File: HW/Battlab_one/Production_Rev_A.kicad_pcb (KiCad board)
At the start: 2 copper layers, 68.1 x 50.5 mm, 51 parts, among them IC2 MIC5225-5.0YM5-TR, J1 BANANA_CONN, J3 BANANA_CONN, P1 USB_C_Plug, T1 750315371

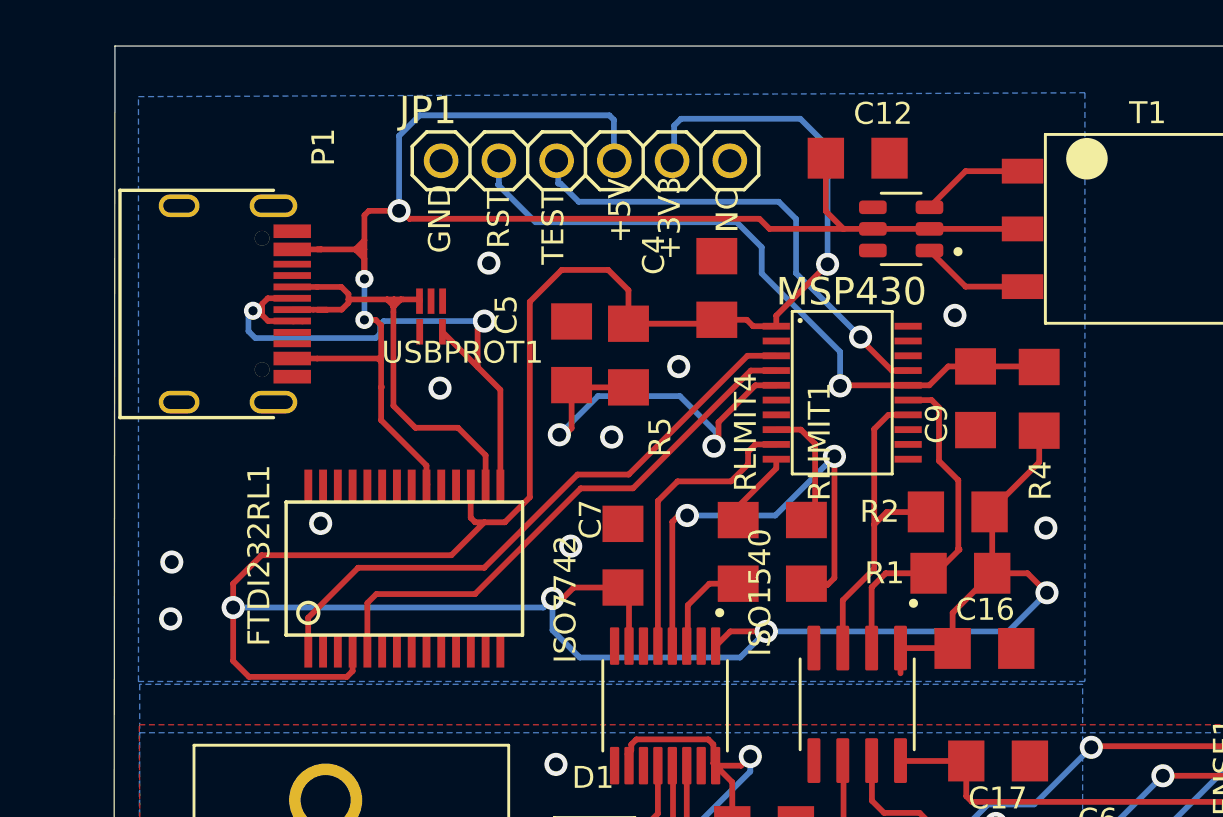
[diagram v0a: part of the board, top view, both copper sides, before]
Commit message: USB-C resistor
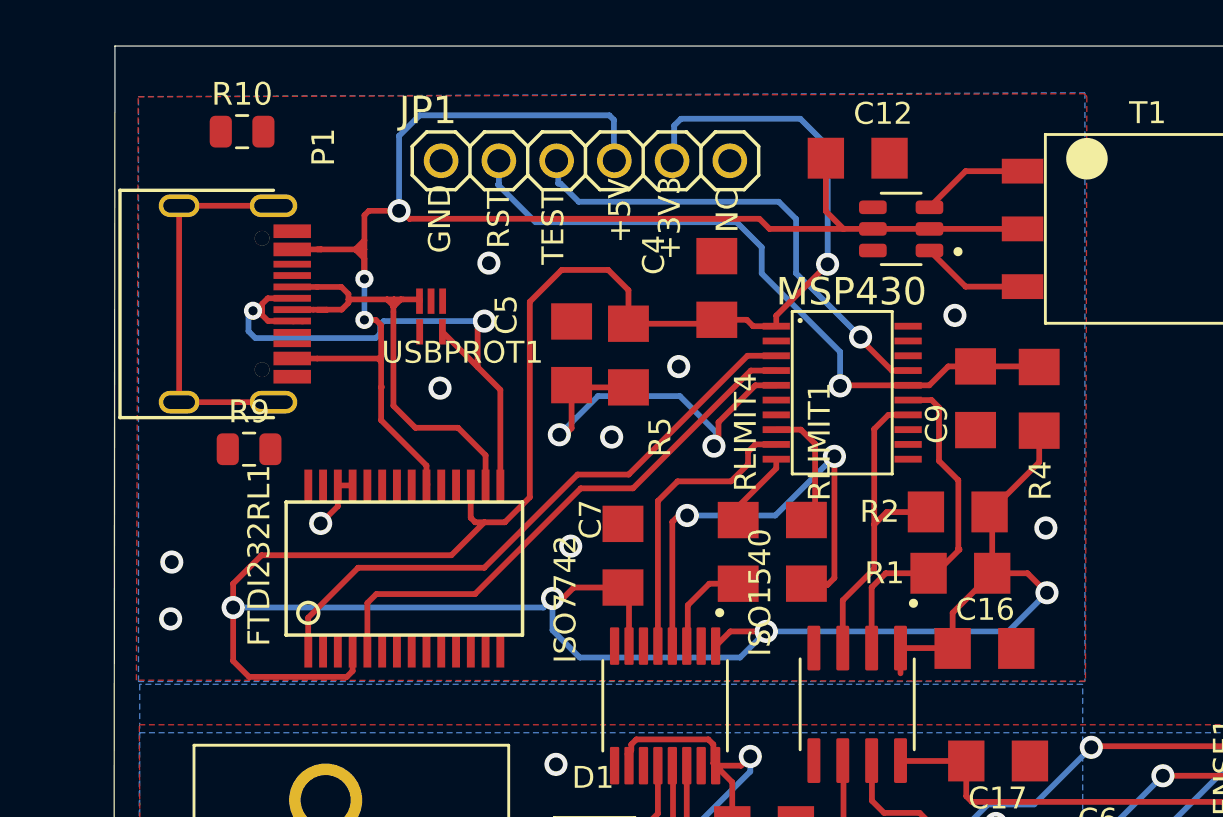
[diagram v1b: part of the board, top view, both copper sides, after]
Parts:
- added R10: 5.1K, Resistor_SMD:R_0805_2012Metric, F.Cu at (120.1, 83.5)
- added R9: 5.1K, Resistor_SMD:R_0805_2012Metric, F.Cu at (120.4, 97.5)
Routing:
- net Net-(P1-PadS1): track 0.00 -> 16.9 mm
- net GND: track 0.00 -> 2.67 mm
- added copper zone on F.Cu, net GND

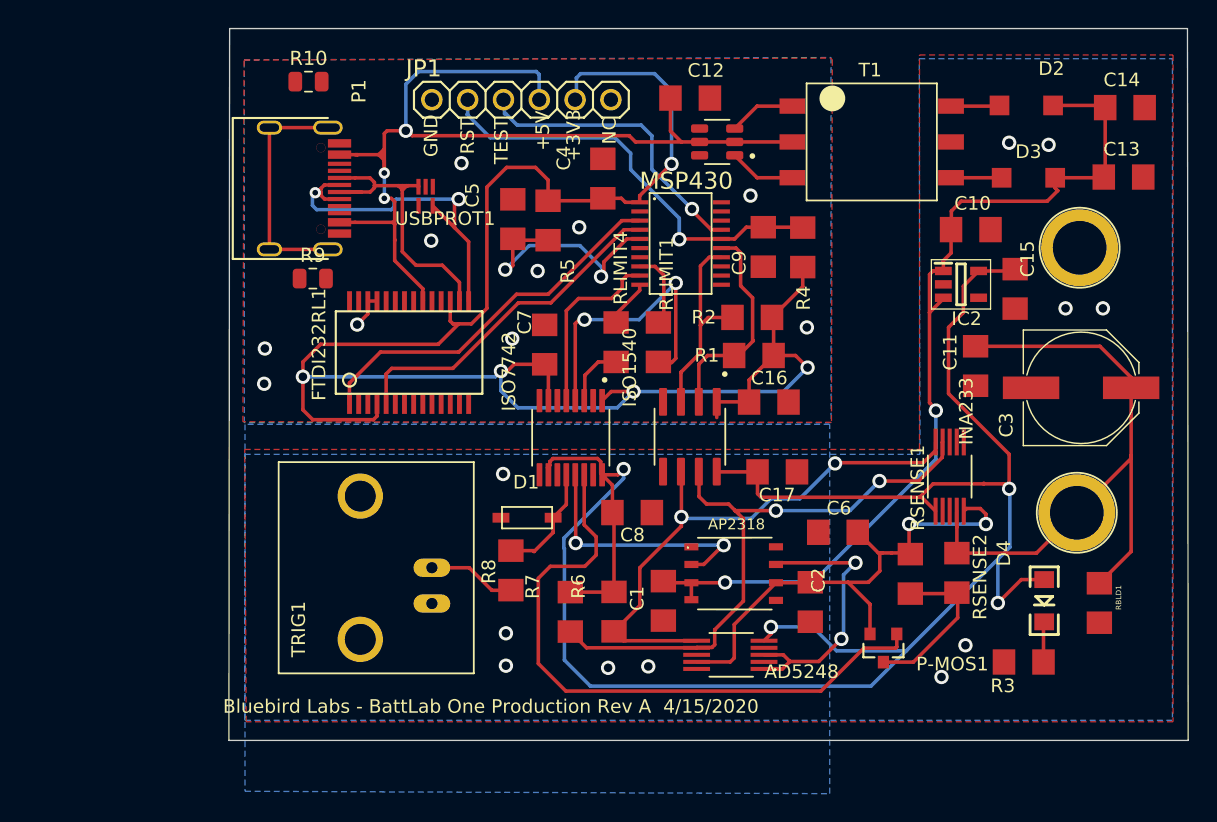
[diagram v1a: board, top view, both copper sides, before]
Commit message: Usb c fixed RTC 0 unconnect
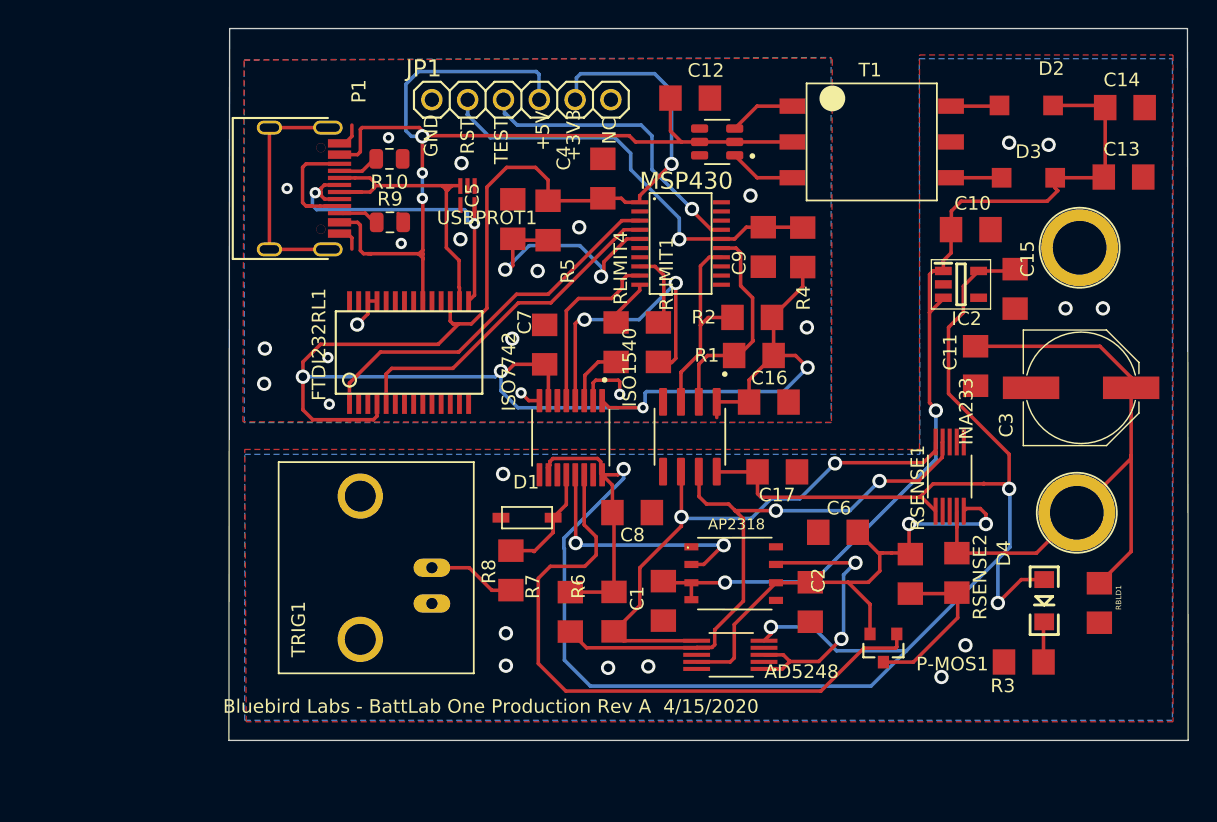
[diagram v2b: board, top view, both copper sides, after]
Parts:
- moved R10 7.94 mm to (125.9, 89.0), turned to 180 degrees
- moved R9 6.77 mm to (125.9, 93.5)
- moved USBPROT1 2.97 mm to (131.4, 91.6)
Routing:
- net GND: track 2.67 -> 12.2 mm, vias 10 -> 17
- net (no net): track 0.00 -> 9.32 mm
- net /VBUS: track 70.8 -> 75.1 mm
- net Net-(P1-PadB5): track 0.00 -> 3.00 mm
- net Net-(P1-PadA5): track 0.00 -> 2.85 mm
- net /D+: track 26.3 -> 24.7 mm
- net Net-(C16-Pad1): track 132.1 -> 133.2 mm
- net /D-: track 21.2 -> 21.9 mm

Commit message: Silkscreen moved
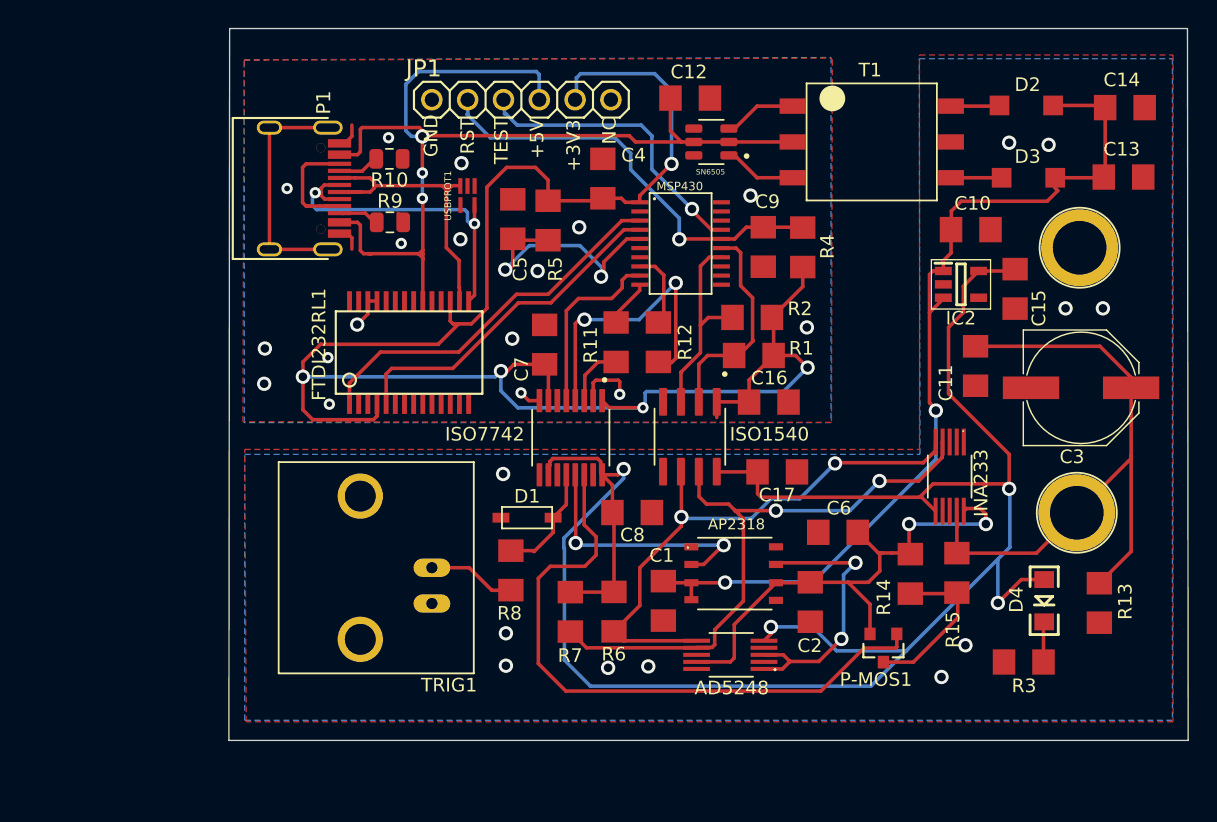
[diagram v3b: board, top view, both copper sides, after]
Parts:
- moved SN6505 0.41 mm to (148.7, 87.8)
- renumbered RLIMIT4 to R11, RLIMIT1 to R12, RBLD1 to R13, RSENSE1 to R14, RSENSE2 to R15
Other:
- board text removed: "Bluebird Labs - BattLab One Production Rev A 4/15/2020"
